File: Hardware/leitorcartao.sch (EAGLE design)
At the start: 156 parts, among them IC1 TL084, IC2 TL084, Q1 DMN3404, Q4 BC847ALT1SMD, Q5 BC847ALT1SMD, Q6 BC847ALT1SMD, Q7 BC847ALT1SMD, Q8 MMBT4403, Q9 MMBT4401, U1 SAMD20E14A-AUT, U3 TLV1117-50CDCYR, U4 MFRC52202HN1, U5 LP2985-33DBVR, X1 ANTENA, X2 MIFARE ANTENA

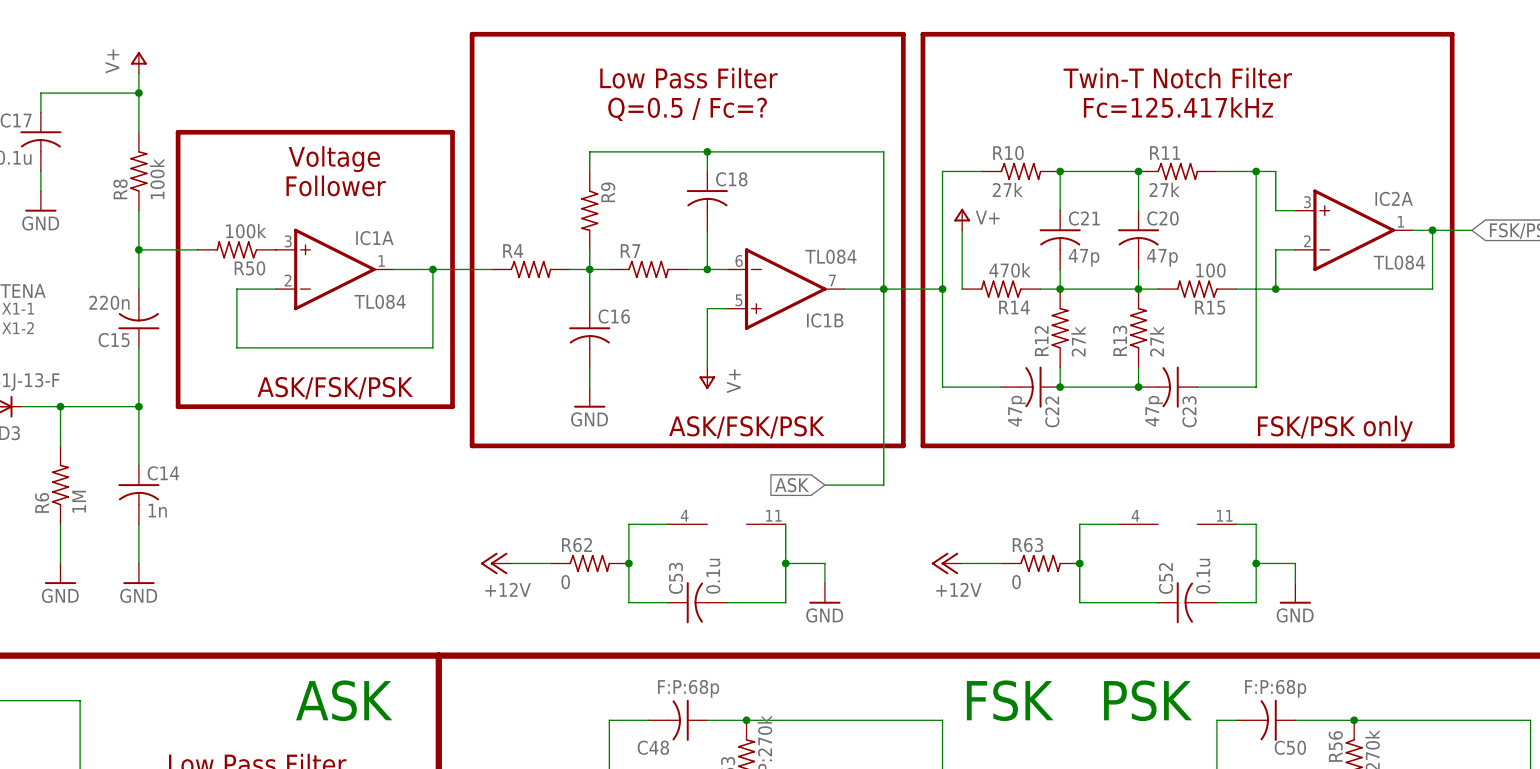
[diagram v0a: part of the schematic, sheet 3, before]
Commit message: Adicionadas duas novas camadas na placa.
Layer 4 -> Power Plane
Layer 5 -> Ground Plane
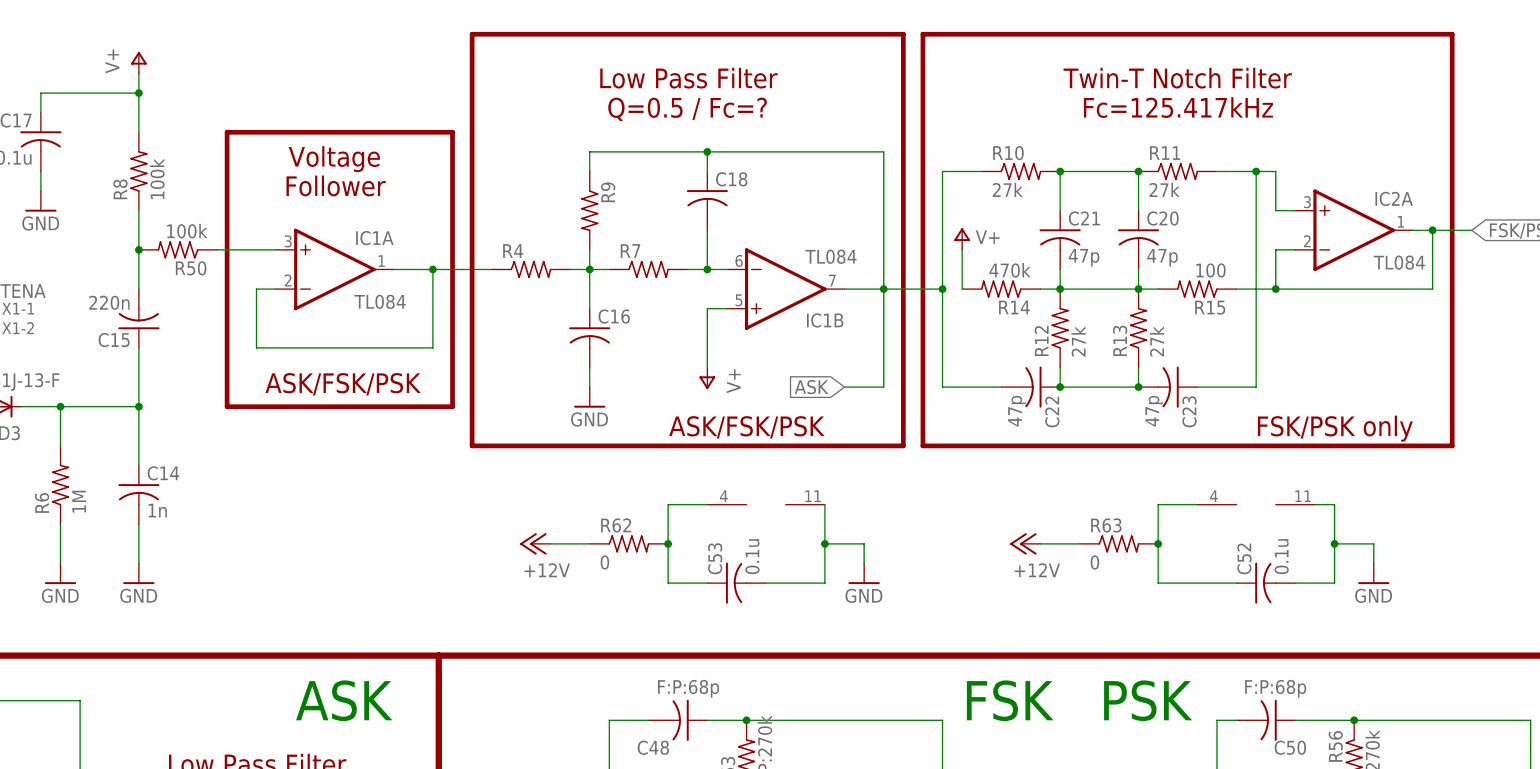
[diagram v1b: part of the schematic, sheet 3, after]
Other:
- moved on the sheet: C52, C53, R50, R62, R63

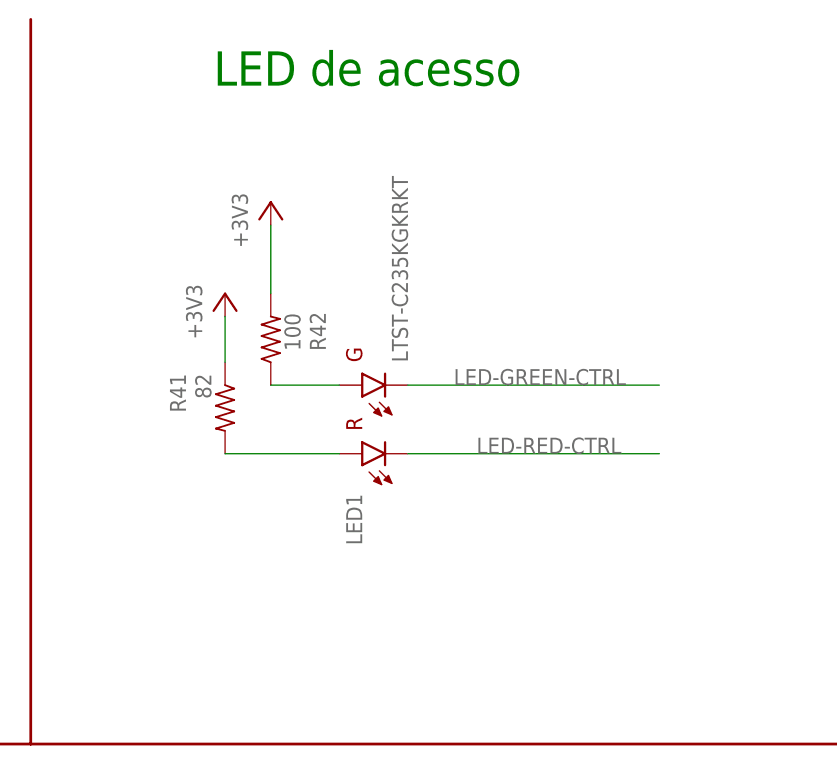
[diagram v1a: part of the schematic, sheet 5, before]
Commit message: Mudanças na placa.
Inclusão do LED Red/Green.
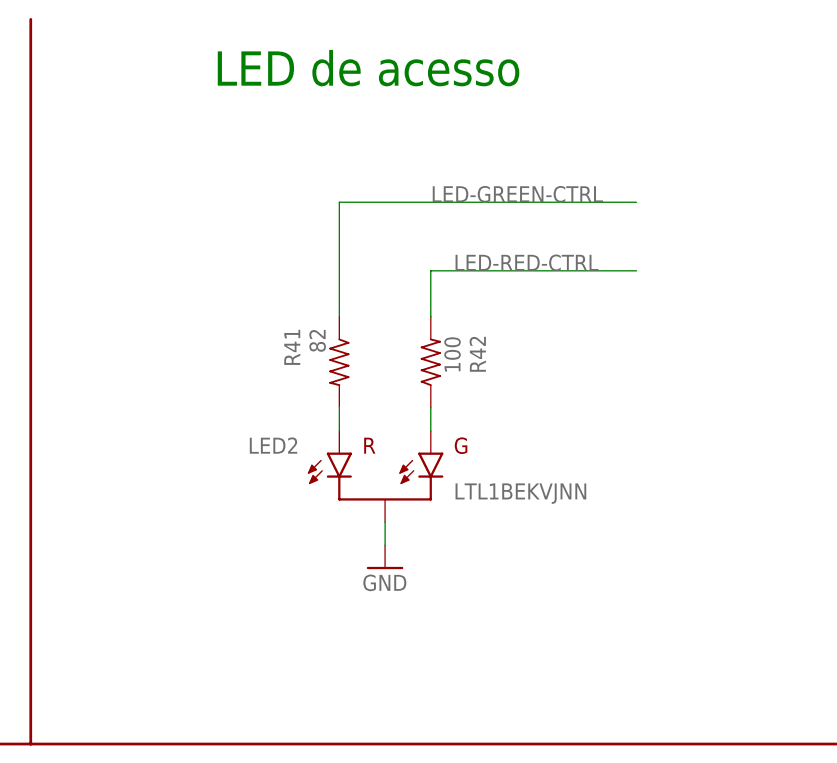
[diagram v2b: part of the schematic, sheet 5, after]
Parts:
- removed LED1: LTST-C235KGKRKT, RFiD:LTST-C235KGKRKT
- added LED2: LTL1BEKVJNN, RFiD:LTL1BEKVJNN
- R14: value 470k -> 470
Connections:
- net +3V3: no longer R41.1, R42.2
- net GND: now also LED2.COMMON
- net LED-GREEN-CTRL: now also R41.1; no longer LED1.1
- net LED-RED-CTRL: now also R42.2; no longer LED1.4
- net N$52: now also LED2.ANODE_RED; no longer LED1.3
- net N$53: now also LED2.ANODE_GRN; no longer LED1.2
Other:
- moved on the sheet: R41, R42
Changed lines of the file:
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@@
 <attribute name="CUSTOMER_PN" value="R/180/5%/04"/>
 </part>
-<part name="+3V14" library="supply1" deviceset="+3V3" device=""/>
-<part name="+3V15" library="supply1" deviceset="+3V3" device=""/>
 <part name="SG1" library="RFiD" deviceset="F/TMB" device="">
 <attribute name="CUSTOMER_PN" value="BUZZER"/>
@@
 </part>
 <part name="GND59" library="supply1" deviceset="GND" device=""/>
-<part name="LED1" library="RFiD" deviceset="LTST-C235KGKRKT" device=""/>
 <part name="C12" library="RFiD" deviceset="C-US" device="C1812" value="1n"/>
 <part name="GND20" library="supply1" deviceset="GND" device=""/>
@@
 <part name="Q8" library="RFiD" deviceset="MMBT4403" device=""/>
 <part name="Q9" library="RFiD" deviceset="MMBT4401" device=""/>
-<part name="R14" library="RFiD" deviceset="R-US_" device="R0402" value="470k">
+<part name="R14" library="RFiD" deviceset="R-US_" device="R0402" value="470">
 <attribute name="CUSTOMER_PN" value="R/1M/5%/04"/>
 </part>
@@
 <part name="P+19" library="supply1" deviceset="V+" device=""/>
 <part name="P+20" library="supply1" deviceset="V+" device=""/>
+<part name="LED2" library="RFiD" deviceset="LTL1BEKVJNN" device=""/>
+<part name="GND19" library="supply1" deviceset="GND" device=""/>
 </parts>
 <sheets>
@@
 <instance part="+3V12" gate="G$1" x="185.42" y="162.56"/>
 <instance part="+3V13" gate="G$1" x="185.42" y="132.08"/>
-<instance part="R41" gate="G$1" x="88.9" y="132.08" smashed="yes" rot="R270">
-<attribute name="NAME" x="82.7786" y="135.89" size="1.778" layer="95" rot="R270"/>
-<attribute name="VALUE" x="85.598" y="135.89" size="1.778" layer="96" rot="R270"/>
-<attribute name="CUSTOMER_PN" x="88.9" y="132.08" size="1.778" layer="96" display="off"/>
-</instance>
-<instance part="R42" gate="G$1" x="93.98" y="139.7" smashed="yes" rot="R90">
-<attribute name="NAME" x="100.1014" y="138.43" size="1.778" layer="95" rot="R90"/>
-<attribute name="VALUE" x="97.282" y="138.43" size="1.778" layer="96" rot="R90"/>
-<attribute name="CUSTOMER_PN" x="93.98" y="139.7" size="1.778" layer="96" display="off"/>
-</instance>
-<instance part="+3V14" gate="G$1" x="88.9" y="144.78"/>
-<instance part="+3V15" gate="G$1" x="93.98" y="154.94"/>
+<instance part="R41" gate="G$1" x="101.6" y="137.16" smashed="yes" rot="R270">
+<attribute name="NAME" x="95.4786" y="140.97" size="1.778" layer="95" rot="R270"/>
+<attribute name="VALUE" x="98.298" y="140.97" size="1.778" layer="96" rot="R270"/>
+<attribute name="CUSTOMER_PN" x="101.6" y="137.16" size="1.778" layer="96" display="off"/>
+</instance>
+<instance part="R42" gate="G$1" x="111.76" y="137.16" smashed="yes" rot="R90">
+<attribute name="NAME" x="117.8814" y="135.89" size="1.778" layer="95" rot="R90"/>
+<attribute name="VALUE" x="115.062" y="135.89" size="1.778" layer="96" rot="R90"/>
+<attribute name="CUSTOMER_PN" x="111.76" y="137.16" size="1.778" layer="96" display="off"/>
+</instance>
 <instance part="SG1" gate="1" x="48.26" y="142.24" rot="R270">
 <attribute name="CUSTOMER_PN" x="48.26" y="142.24" size="1.778" layer="96" display="off"/>
@@
 <instance part="SJ?1" gate="G$1" x="35.56" y="154.94" rot="R180"/>
 <instance part="P+16" gate="1" x="48.26" y="162.56"/>
-<instance part="LED1" gate="G$1" x="106.68" y="132.08" rot="R90"/>
+<instance part="LED2" gate="G$1" x="109.22" y="124.46"/>
+<instance part="GND19" gate="1" x="106.68" y="114.3"/>
 </instances>
 <busses>
@@
 <wire x1="213.36" y1="127" x2="218.44" y2="127" width="0.1524" layer="91"/>
 <wire x1="218.44" y1="127" x2="218.44" y2="124.46" width="0.1524" layer="91"/>
+</segment>
+<segment>
+<pinref part="LED2" gate="G$1" pin="COMMON"/>
+<pinref part="GND19" gate="1" pin="GND"/>
+<wire x1="106.68" y1="116.84" x2="106.68" y2="119.38" width="0.1524" layer="91"/>
 </segment>
 </net>
@@
 </segment>
 <segment>
-<pinref part="R41" gate="G$1" pin="1"/>
-<pinref part="+3V14" gate="G$1" pin="+3V3"/>
-<wire x1="88.9" y1="137.16" x2="88.9" y2="142.24" width="0.1524" layer="91"/>
-</segment>
-<segment>
-<pinref part="R42" gate="G$1" pin="2"/>
-<wire x1="93.98" y1="144.78" x2="93.98" y2="152.4" width="0.1524" layer="91"/>
-<pinref part="+3V15" gate="G$1" pin="+3V3"/>
-</segment>
-<segment>
 <pinref part="D5" gate="G$1" pin="C2"/>
 <pinref part="+3V18" gate="G$1" pin="+3V3"/>
@@
 <wire x1="25.4" y1="160.02" x2="25.4" y2="154.94" width="0.1524" layer="91"/>
 <wire x1="25.4" y1="154.94" x2="30.48" y2="154.94" width="0.1524" layer="91"/>
-</segment>
-</net>
-<net name="N$52" class="0">
-<segment>
-<pinref part="R41" gate="G$1" pin="2"/>
-<wire x1="88.9" y1="127" x2="101.6" y2="127" width="0.1524" layer="91"/>
-<pinref part="LED1" gate="G$1" pin="3"/>
-</segment>
-</net>
-<net name="N$53" class="0">
-<segment>
-<pinref part="R42" gate="G$1" pin="1"/>
-<wire x1="93.98" y1="134.62" x2="101.6" y2="134.62" width="0.1524" layer="91"/>
-<pinref part="LED1" gate="G$1" pin="2"/>
 </segment>
 </net>
@@
 <net name="LED-GREEN-CTRL" class="0">
 <segment>
-<wire x1="109.22" y1="134.62" x2="137.16" y2="134.62" width="0.1524" layer="91"/>
-<label x="114.3" y="134.62" size="1.778" layer="95"/>
-<pinref part="LED1" gate="G$1" pin="1"/>
+<wire x1="101.6" y1="154.94" x2="134.62" y2="154.94" width="0.1524" layer="91"/>
+<label x="111.76" y="154.94" size="1.778" layer="95"/>
+<pinref part="R41" gate="G$1" pin="1"/>
+<wire x1="101.6" y1="154.94" x2="101.6" y2="142.24" width="0.1524" layer="91"/>
 </segment>
 </net>
 <net name="LED-RED-CTRL" class="0">
 <segment>
-<wire x1="137.16" y1="127" x2="109.22" y2="127" width="0.1524" layer="91"/>
-<label x="116.84" y="127" size="1.778" layer="95"/>
-<pinref part="LED1" gate="G$1" pin="4"/>
+<wire x1="134.62" y1="147.32" x2="111.76" y2="147.32" width="0.1524" layer="91"/>
+<label x="114.3" y="147.32" size="1.778" layer="95"/>
+<pinref part="R42" gate="G$1" pin="2"/>
+<wire x1="111.76" y1="147.32" x2="111.76" y2="142.24" width="0.1524" layer="91"/>
 </segment>
 </net>
@@
 </segment>
 </net>
+<net name="N$52" class="0">
+<segment>
+<pinref part="LED2" gate="G$1" pin="ANODE_RED"/>
+<pinref part="R41" gate="G$1" pin="2"/>
+<wire x1="101.6" y1="129.54" x2="101.6" y2="132.08" width="0.1524" layer="91"/>
+</segment>
+</net>
+<net name="N$53" class="0">
+<segment>
+<pinref part="LED2" gate="G$1" pin="ANODE_GRN"/>
+<pinref part="R42" gate="G$1" pin="1"/>
+<wire x1="111.76" y1="129.54" x2="111.76" y2="132.08" width="0.1524" layer="91"/>
+</segment>
+</net>

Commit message: Mudanças no layout.
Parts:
- removed X2: MIFARE ANTENA, con-molex:22-23-2021
- added C13, C58: 0.1u, RFiD:C-USC0402
- added X3: ANTENA, RFiD:22-23-2021
- added Y2: (no value), RFiD:CRYSTALHC49S
- D1: value (none) -> BYG20J; device RFiD:DIODE-DO214AA -> RFiD:BYG20J; CUSTOMER_PN D/SERIE/SMB -> (none)
- D3: value US1J-13-F -> BYG20J; device RFiD:US1J-13-F -> RFiD:BYG20J
- SWD: device pinhead:PINHD-1X5 -> RFiD:PINHD-1X5
- X1: value ANTENA -> MIFARE; device con-molex:22-23-2021 -> RFiD:22-23-2021; CUSTOMER_PN - -> (none)
- renumbered QZ1 to Y1
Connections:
- new net XIN: C58.1, U1IO.PA14, Y2.1
- new net XOUT: C13.1, U1IO.PA15, Y2.2
- net +12V: now also D1.K; no longer D1.C
- net GND: now also C13.2, C58.2
- net N$11: now also X3-1.S; no longer X1-1.S
- net N$38: now also X1-1.S; no longer X2-2.S
- net N$39: now also X1-2.S; no longer X2-1.S
- net N$9: now also X3-2.S; no longer X1-2.S
- net USART-RX: no longer U1IO.PA14
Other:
- note added: "Crystal"
- moved on the sheet: R23, SWD

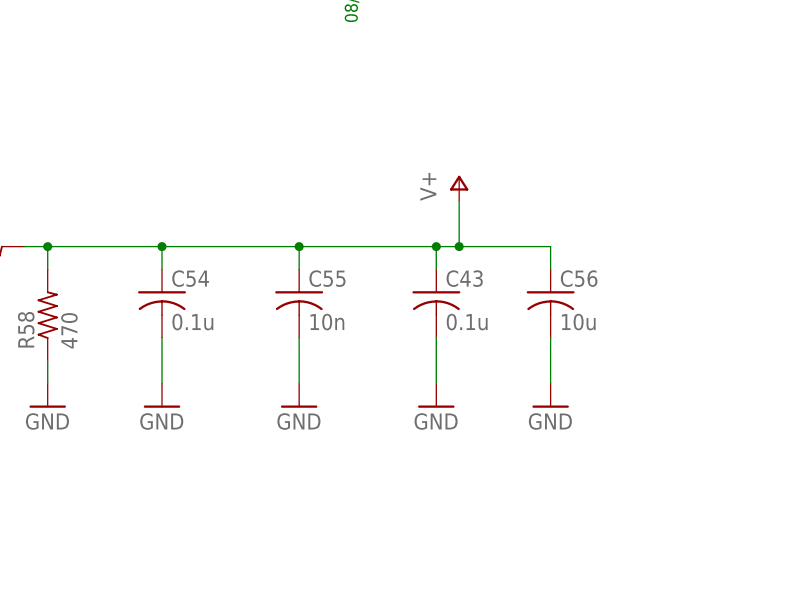
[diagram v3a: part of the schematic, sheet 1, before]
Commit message: Nova versão do roteamento. Tentativa de isolar tudo no top para DFM.
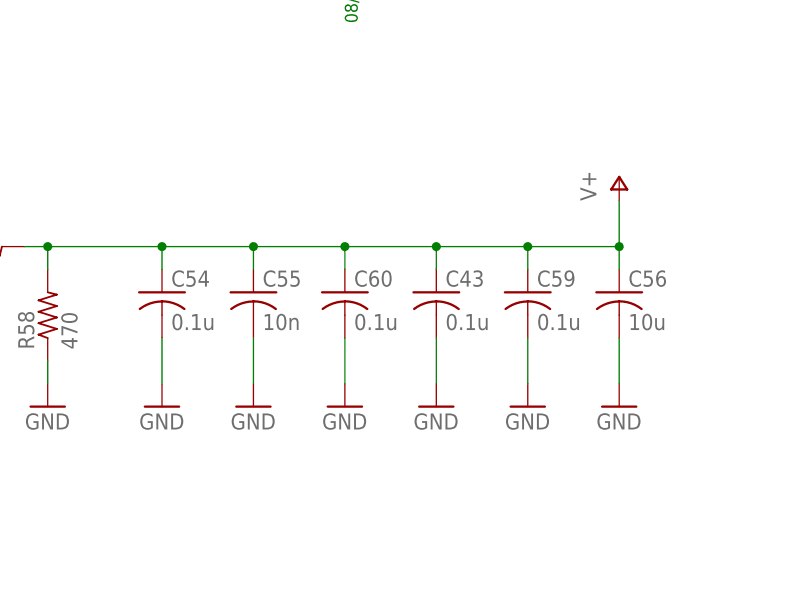
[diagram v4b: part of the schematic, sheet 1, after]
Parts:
- added C59, C60: 0.1u, RFiD:C-USC0402
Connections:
- net GND: now also C59.2, C60.2
- net V+: now also C59.1, C60.1
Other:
- moved on the sheet: C55, C56
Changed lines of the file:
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@@
 <part name="GND26" library="supply1" deviceset="GND" device=""/>
 <part name="X1" library="RFiD" deviceset="22-23-2021" device="" value="MIFARE"/>
+<part name="C59" library="RFiD" deviceset="C-US" device="C0402" value="0.1u"/>
+<part name="GND28" library="supply1" deviceset="GND" device=""/>
+<part name="C60" library="RFiD" deviceset="C-US" device="C0402" value="0.1u"/>
+<part name="GND30" library="supply1" deviceset="GND" device=""/>
 </parts>
 <sheets>
@@
 <instance part="GND34" gate="1" x="175.26" y="53.34"/>
 <instance part="C54" gate="G$1" x="187.96" y="66.04"/>
-<instance part="C55" gate="G$1" x="203.2" y="66.04"/>
+<instance part="C55" gate="G$1" x="198.12" y="66.04"/>
 <instance part="GND35" gate="1" x="187.96" y="53.34"/>
-<instance part="GND52" gate="1" x="203.2" y="53.34"/>
-<instance part="P+15" gate="1" x="220.98" y="78.74"/>
+<instance part="GND52" gate="1" x="198.12" y="53.34"/>
+<instance part="P+15" gate="1" x="238.76" y="78.74"/>
 <instance part="P+12" gate="1" x="157.48" y="76.2"/>
 <instance part="C43" gate="G$1" x="218.44" y="66.04"/>
 <instance part="GND1" gate="1" x="218.44" y="53.34"/>
-<instance part="C56" gate="G$1" x="231.14" y="66.04"/>
-<instance part="GND58" gate="1" x="231.14" y="53.34"/>
+<instance part="C56" gate="G$1" x="238.76" y="66.04"/>
+<instance part="GND58" gate="1" x="238.76" y="53.34"/>
 <instance part="D1" gate="G$1" x="76.2" y="124.46" rot="R180"/>
+<instance part="C59" gate="G$1" x="228.6" y="66.04"/>
+<instance part="GND28" gate="1" x="228.6" y="53.34"/>
+<instance part="C60" gate="G$1" x="208.28" y="66.04"/>
+<instance part="GND30" gate="1" x="208.28" y="53.34"/>
 </instances>
 <busses>
@@
 <pinref part="GND52" gate="1" pin="GND"/>
 <pinref part="C55" gate="G$1" pin="2"/>
-<wire x1="203.2" y1="55.88" x2="203.2" y2="60.96" width="0.1524" layer="91"/>
+<wire x1="198.12" y1="55.88" x2="198.12" y2="60.96" width="0.1524" layer="91"/>
 </segment>
 <segment>
@@
 <pinref part="GND58" gate="1" pin="GND"/>
 <pinref part="C56" gate="G$1" pin="2"/>
-<wire x1="231.14" y1="55.88" x2="231.14" y2="60.96" width="0.1524" layer="91"/>
+<wire x1="238.76" y1="55.88" x2="238.76" y2="60.96" width="0.1524" layer="91"/>
+</segment>
+<segment>
+<pinref part="C59" gate="G$1" pin="2"/>
+<pinref part="GND28" gate="1" pin="GND"/>
+<wire x1="228.6" y1="60.96" x2="228.6" y2="55.88" width="0.1524" layer="91"/>
+</segment>
+<segment>
+<pinref part="GND30" gate="1" pin="GND"/>
+<pinref part="C60" gate="G$1" pin="2"/>
+<wire x1="208.28" y1="55.88" x2="208.28" y2="60.96" width="0.1524" layer="91"/>
 </segment>
 </net>
@@
 <net name="V+" class="0">
 <segment>
+<pinref part="C56" gate="G$1" pin="1"/>
+<pinref part="P+15" gate="1" pin="V+"/>
+<wire x1="238.76" y1="76.2" x2="238.76" y2="71.12" width="0.1524" layer="91"/>
 <pinref part="R57" gate="G$1" pin="2"/>
 <pinref part="R58" gate="G$1" pin="2"/>
+<wire x1="238.76" y1="71.12" x2="238.76" y2="68.58" width="0.1524" layer="91"/>
 <wire x1="172.72" y1="71.12" x2="175.26" y2="71.12" width="0.1524" layer="91"/>
 <wire x1="175.26" y1="71.12" x2="175.26" y2="68.58" width="0.1524" layer="91"/>
@@
 <wire x1="187.96" y1="71.12" x2="187.96" y2="68.58" width="0.1524" layer="91"/>
 <pinref part="C55" gate="G$1" pin="1"/>
-<wire x1="187.96" y1="71.12" x2="203.2" y2="71.12" width="0.1524" layer="91"/>
-<wire x1="203.2" y1="71.12" x2="203.2" y2="68.58" width="0.1524" layer="91"/>
+<wire x1="187.96" y1="71.12" x2="198.12" y2="71.12" width="0.1524" layer="91"/>
+<wire x1="198.12" y1="71.12" x2="198.12" y2="68.58" width="0.1524" layer="91"/>
 <junction x="187.96" y="71.12"/>
-<wire x1="203.2" y1="71.12" x2="218.44" y2="71.12" width="0.1524" layer="91"/>
-<junction x="203.2" y="71.12"/>
-<pinref part="P+15" gate="1" pin="V+"/>
-<wire x1="218.44" y1="71.12" x2="220.98" y2="71.12" width="0.1524" layer="91"/>
-<wire x1="220.98" y1="71.12" x2="220.98" y2="76.2" width="0.1524" layer="91"/>
+<wire x1="198.12" y1="71.12" x2="208.28" y2="71.12" width="0.1524" layer="91"/>
+<junction x="198.12" y="71.12"/>
 <pinref part="C43" gate="G$1" pin="1"/>
+<wire x1="208.28" y1="71.12" x2="218.44" y2="71.12" width="0.1524" layer="91"/>
 <wire x1="218.44" y1="68.58" x2="218.44" y2="71.12" width="0.1524" layer="91"/>
+<pinref part="C59" gate="G$1" pin="1"/>
+<wire x1="228.6" y1="68.58" x2="228.6" y2="71.12" width="0.1524" layer="91"/>
+<wire x1="218.44" y1="71.12" x2="228.6" y2="71.12" width="0.1524" layer="91"/>
 <junction x="218.44" y="71.12"/>
-<pinref part="C56" gate="G$1" pin="1"/>
-<wire x1="220.98" y1="71.12" x2="231.14" y2="71.12" width="0.1524" layer="91"/>
-<wire x1="231.14" y1="71.12" x2="231.14" y2="68.58" width="0.1524" layer="91"/>
-<junction x="220.98" y="71.12"/>
-</segment>
-</net>
+<wire x1="228.6" y1="71.12" x2="238.76" y2="71.12" width="0.1524" layer="91"/>
+<junction x="228.6" y="71.12"/>
+<junction x="238.76" y="71.12"/>
+<pinref part="C60" gate="G$1" pin="1"/>
+<wire x1="208.28" y1="68.58" x2="208.28" y2="71.12" width="0.1524" layer="91"/>
+<junction x="208.28" y="71.12"/>
+</segment>
+</net>
